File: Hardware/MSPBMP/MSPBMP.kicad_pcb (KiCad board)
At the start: 2 copper layers, 73.7 x 38.1 mm, 63 parts, among them J1 USB_B_Micro, J2 SWD, J3 RS232, J4 JTAG, J5 ISP, U1 AMS1117-3.3, U2 STM32F103CBT6, U3 AD8531ARTZ, U4 TXS0108EPWR, Y1 8MHz

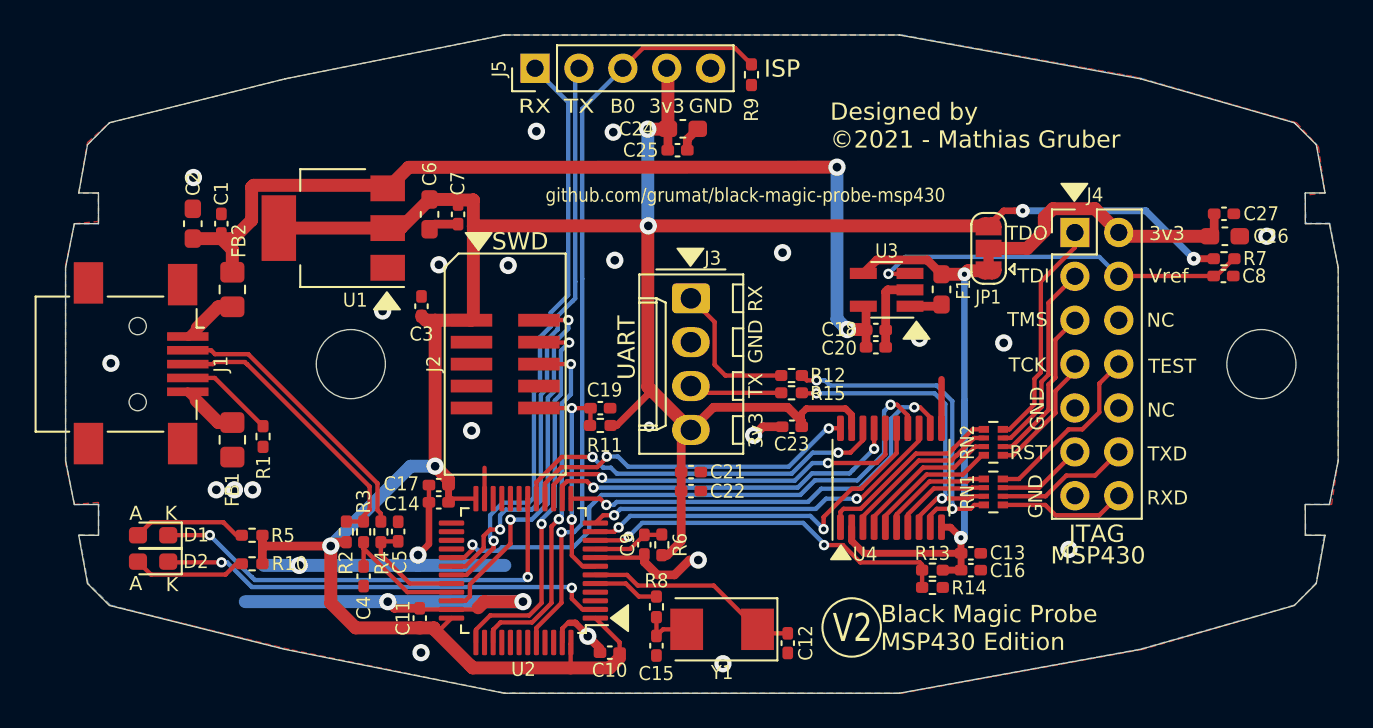
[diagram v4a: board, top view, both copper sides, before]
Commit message: Hardware V2 improvements (component values and sizes, layout and review of V-Target circuitry).
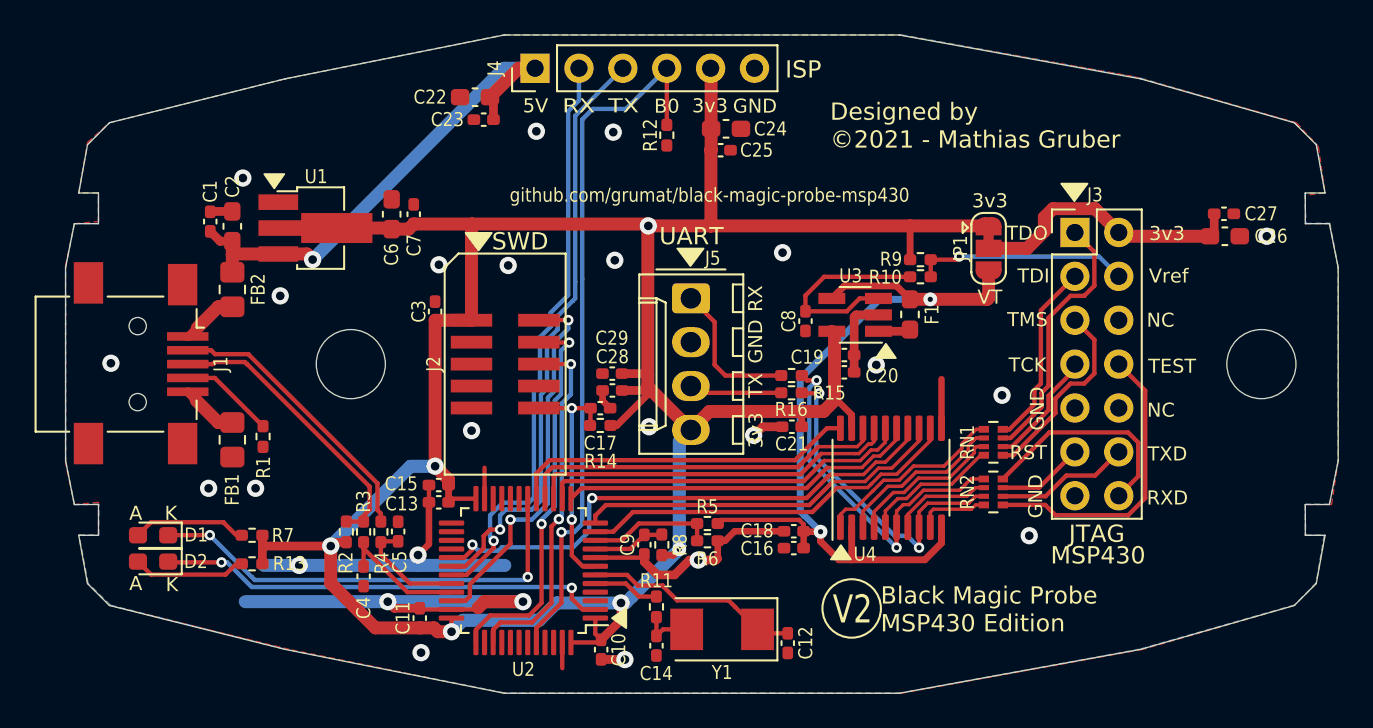
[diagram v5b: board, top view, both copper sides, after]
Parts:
- removed the R9 at (103.2, 53.1)
- added C22: 10uF, Capacitor_SMD:C_0603_1608Metric_Pad1.08x0.95mm_HandSolder, F.Cu at (87.2, 54.4)
- added C23: 100nF, Capacitor_SMD:C_0402_1005Metric_Pad0.74x0.62mm_HandSolder, F.Cu at (87.7, 55.7)
- added R10: 4k7, Resistor_SMD:R_0402_1005Metric_Pad0.72x0.64mm_HandSolder, F.Cu at (113.0, 64.8)
- added R12: 100K, Resistor_SMD:R_0402_1005Metric_Pad0.72x0.64mm_HandSolder, F.Cu at (98.3, 56.6)
- J4: renamed from J5; footprint Connector_PinHeader_2.54mm:PinHeader_1x05_P2.54mm_Vertical -> Connector_PinHeader_2.54mm:PinHeader_1x06_P2.54mm_Vertical
- U1: footprint Package_TO_SOT_SMD:SOT-223-3_TabPin2 -> Package_TO_SOT_SMD:SOT-89-3_Handsoldering
- moved C8 24.3 mm to (106.3, 67.4), turned to 90 degrees
- moved R9 17.6 mm to (113.0, 63.8)
- moved R5 13.3 mm to (100.7, 79.1)
- moved R6 13.3 mm to (100.7, 80.1)
- moved C18 10.5 mm to (105.7, 79.5), turned to 180 degrees
- moved C16 10.3 mm to (105.7, 80.5), turned to 180 degrees
- moved C29 8.19 mm to (95.1, 70.4), turned to 180 degrees
- moved C28 6.56 mm to (95.2, 71.4), turned to 180 degrees
- moved C7 2.57 mm to (83.7, 61.2), turned to 90 degrees
- moved C24 2.50 mm to (101.7, 56.2)
- moved C25 2.50 mm to (101.4, 57.5)
- moved C19 2.33 mm to (108.6, 69.3)
- moved C20 2.33 mm to (108.6, 70.3)
- moved U3 2.33 mm to (109.2, 67.0)
- moved F1 2.33 mm to (112.4, 67.0)
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- renumbered C14 to C13, C15 to C14, C17 to C15, C13 to C16, C19 to C17, C16 to C18, C18 to C19, C23 to C21, C21 to C28, C22 to C29, J4 to J3, J3 to J5, R8 to R11, R10 to R13, R11 to R14, R12 to R15, R15 to R16, R13 to R5, R14 to R6, R5 to R7, R6 to R8, R7 to R9, RN2 to RN1, RN1 to RN2
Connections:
- C19 pad 1: +5V -> +3V3
- C20 pad 2: +5V -> +3V3
- C8 pad 2: /TVCC -> Net-(C8-Pad2)
- J4 pad 1: /ISP_RX -> +5V
- J4 pad 2: /ISP_TX -> /ISP_RX
- J4 pad 3: /BOOT0 -> /ISP_TX
- J4 pad 4: +3V3 -> /BOOT0
- J4 pad 5: GND -> +3V3
- JP1 pad 1: /VCC_TOOL -> +3V3
- JP1 pad 3: +3V3 -> /VCC_TOOL
- RN1 pad 1: /LTDO -> /LTDI
- RN1 pad 2: /LTDI -> /LTDO
- RN1 pad 3: /LTMS -> /LTCK
- RN1 pad 4: /LTCK -> /LTMS
- RN1 pad 5: /TTCK -> /TTMS
- RN1 pad 6: /TTMS -> /TTCK
- RN1 pad 7: /TTDI -> /TTDO
- RN1 pad 8: /TTDO -> /TTDI
- RN2 pad 1: /LTEST -> /LRXD
- RN2 pad 4: /LRXD -> /LTEST
- RN2 pad 5: /TRXD -> /TTEST
- RN2 pad 8: /TTEST -> /TRXD
- U3 pad 3: /TVCC -> Net-(C8-Pad2)
- U3 pad 5: +5V -> +3V3
- U4 pad 1: /LTDO -> /LTDI
- U4 pad 12: /JRXD -> /JTEST
- U4 pad 15: /JTEST -> /JRXD
- U4 pad 16: /JTCK -> /JTMS
- U4 pad 17: /JTMS -> /JTCK
- U4 pad 18: /JTDI -> /JTDO
- U4 pad 20: /JTDO -> /JTDI
- U4 pad 3: /LTDI -> /LTDO
- U4 pad 4: /LTMS -> /LTCK
- U4 pad 5: /LTCK -> /LTMS
- U4 pad 6: /LTEST -> /LRXD
- U4 pad 9: /LRXD -> /LTEST
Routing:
- net +5V: track 55.4 -> 30.3 mm, vias 2 -> 1
- net /VREF2: track 21.7 -> 7.29 mm, vias 2 -> 0
- net /VCC_TOOL: track 35.1 -> 48.9 mm
- net Net-(C8-Pad2): track 0.00 -> 12.0 mm
- net /TVCC: track 22.6 -> 12.4 mm
- net /TTEST: track 10.4 -> 17.3 mm
- net +3V3: track 169.1 -> 163.0 mm
- net /TRXD: track 7.42 -> 12.7 mm
- net /JRXD: track 25.4 -> 20.9 mm, vias 2 -> 0
- net GND: track 64.1 -> 68.4 mm, vias 27 -> 25
- net /BOOT0: track 44.1 -> 41.3 mm
- net /LTEST: track 6.64 -> 4.14 mm
- net /JTDI: track 22.4 -> 20.1 mm, vias 2 -> 0
- net /TTMS: track 9.35 -> 11.3 mm
- net /TTDO: track 13.5 -> 15.5 mm
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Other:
- board text added: "5V"
- board text added: "VT"
